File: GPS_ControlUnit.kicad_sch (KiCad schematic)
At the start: 0 parts

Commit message: MAX-M10S-00B
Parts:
- added ?: MAX-M10S-00B, symbol MAX-M10S-00B:MAX-M10S-00B
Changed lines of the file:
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@@
 (kicad_sch (version 20211123) (generator eeschema)
   (paper "A4")
+  (symbol (lib_id "MAX-M10S-00B:MAX-M10S-00B") (at 213.995 47.625 0) (unit 1)
+    (in_bom yes) (on_board yes) (fields_autoplaced)
+    (property "Reference" "?" (id 0) (at 235.585 34.29 0))
+    (property "Value" "MAX-M10S-00B" (id 1) (at 235.585 36.83 0))
+    (property "Footprint" "" (id 2) (at 213.995 47.625 0)
+      (effects (font (size 1.27 1.27)) hide)
+    )
+    (property "Datasheet" "" (id 3) (at 213.995 47.625 0)
+      (effects (font (size 1.27 1.27)) hide)
+    )
+    (property "Reference_1" "IC" (id 4) (at 235.585 39.37 0))
+    (property "Value_1" "MAX-M10S-00B" (id 5) (at 235.585 41.91 0))
+    (property "Footprint_1" "MAXM10S00B" (id 6) (at 253.365 142.545 0)
+      (effects (font (size 1.27 1.27)) (justify left top) hide)
+    )
+    (property "Datasheet_1" "https://content.u-blox.com/sites/default/files/MAX-M10S_IntegrationManual_UBX-20053088.pdf" (id 7) (at 253.365 242.545 0)
+      (effects (font (size 1.27 1.27)) (justify left top) hide)
+    )
+    (property "Height" "2.7" (id 8) (at 253.365 442.545 0)
+      (effects (font (size 1.27 1.27)) (justify left top) hide)
+    )
+    (property "Manufacturer_Name" "u-blox" (id 9) (at 253.365 542.545 0)
+      (effects (font (size 1.27 1.27)) (justify left top) hide)
+    )
+    (property "Manufacturer_Part_Number" "MAX-M10S-00B" (id 10) (at 253.365 642.545 0)
+      (effects (font (size 1.27 1.27)) (justify left top) hide)
+    )
+    (property "Mouser Part Number" "377-MAX-M10S-00B" (id 11) (at 253.365 742.545 0)
+      (effects (font (size 1.27 1.27)) (justify left top) hide)
+    )
+    (property "Mouser Price/Stock" "https://www.mouser.co.uk/ProductDetail/u-blox/MAX-M10S-00B?qs=A6eO%252BMLsxmT0PfQYPb7LLQ%3D%3D" (id 12) (at 253.365 842.545 0)
+      (effects (font (size 1.27 1.27)) (justify left top) hide)
+    )
+    (property "Arrow Part Number" "MAX-M10S-00B" (id 13) (at 253.365 942.545 0)
+      (effects (font (size 1.27 1.27)) (justify left top) hide)
+    )
+    (property "Arrow Price/Stock" "https://www.arrow.com/en/products/max-m10s-00b/u-blox?region=nac" (id 14) (at 253.365 1042.545 0)
+      (effects (font (size 1.27 1.27)) (justify left top) hide)
+    )
+    (pin "1")
+    (pin "10")
+    (pin "11")
+    (pin "12")
+    (pin "13")
+    (pin "14")
+    (pin "15")
+    (pin "16")
+    (pin "17")
+    (pin "18")
+    (pin "2")
+    (pin "3")
+    (pin "4")
+    (pin "5")
+    (pin "6")
+    (pin "7")
+    (pin "8")
+    (pin "9")
+  )
   (sheet (at 53.34 90.17) (size 59.055 36.195) (fields_autoplaced)
     (stroke (width 0.1524) (type solid) (color 0 0 0 0))

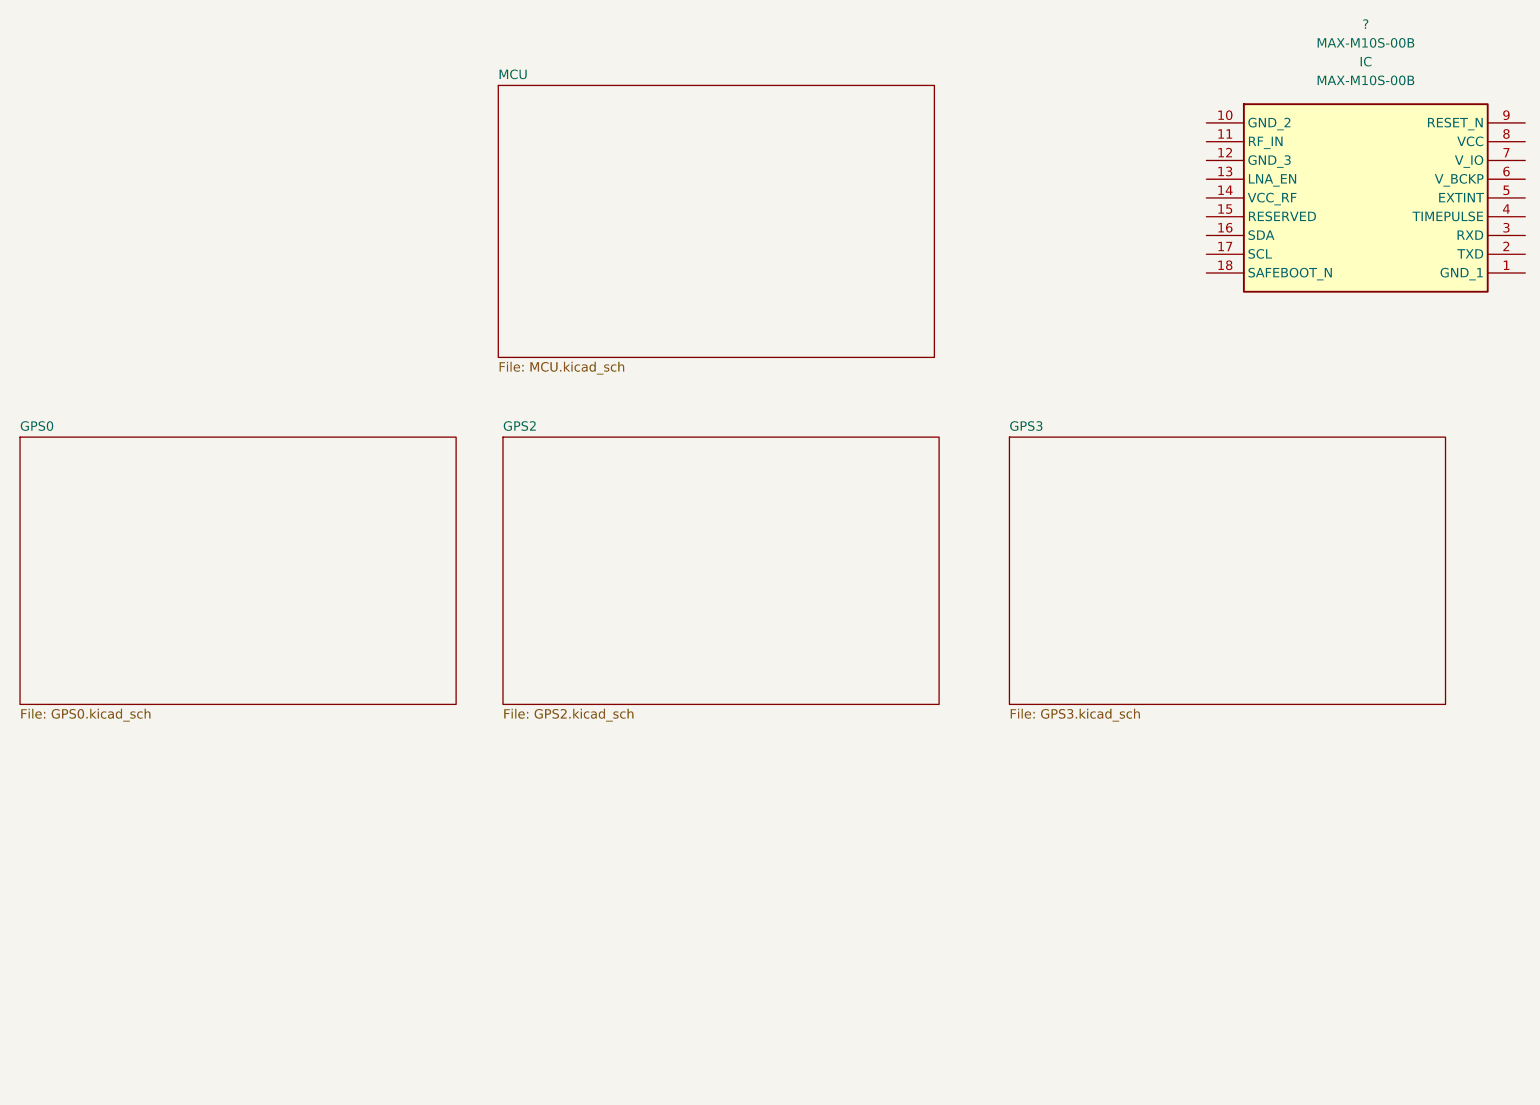
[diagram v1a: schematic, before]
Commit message: Adding M10
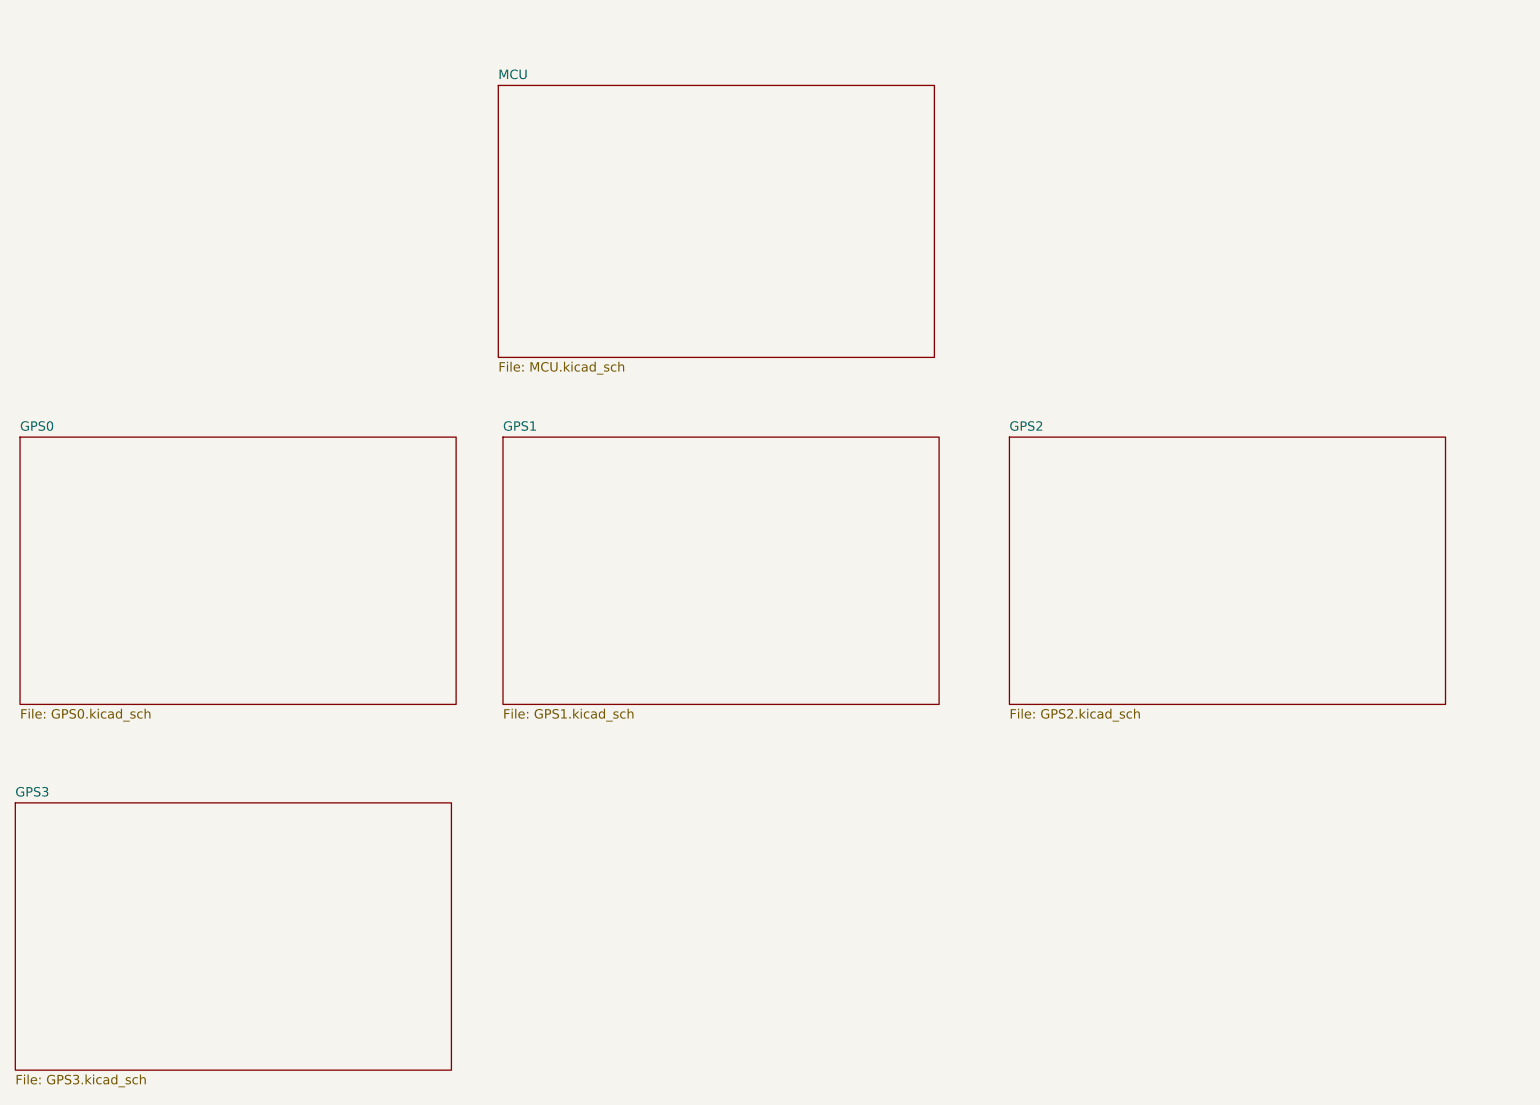
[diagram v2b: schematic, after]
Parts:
- removed ?: MAX-M10S-00B, symbol MAX-M10S-00B:MAX-M10S-00B
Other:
- added sheet GPS1 (GPS1.kicad_sch)
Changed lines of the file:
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@@
 (kicad_sch (version 20211123) (generator eeschema)
   (paper "A4")
-  (symbol (lib_id "MAX-M10S-00B:MAX-M10S-00B") (at 213.995 47.625 0) (unit 1)
-    (in_bom yes) (on_board yes) (fields_autoplaced)
-    (property "Reference" "?" (id 0) (at 235.585 34.29 0))
-    (property "Value" "MAX-M10S-00B" (id 1) (at 235.585 36.83 0))
-    (property "Footprint" "" (id 2) (at 213.995 47.625 0)
-      (effects (font (size 1.27 1.27)) hide)
-    )
-    (property "Datasheet" "" (id 3) (at 213.995 47.625 0)
-      (effects (font (size 1.27 1.27)) hide)
-    )
-    (property "Reference_1" "IC" (id 4) (at 235.585 39.37 0))
-    (property "Value_1" "MAX-M10S-00B" (id 5) (at 235.585 41.91 0))
-    (property "Footprint_1" "MAXM10S00B" (id 6) (at 253.365 142.545 0)
-      (effects (font (size 1.27 1.27)) (justify left top) hide)
-    )
-    (property "Datasheet_1" "https://content.u-blox.com/sites/default/files/MAX-M10S_IntegrationManual_UBX-20053088.pdf" (id 7) (at 253.365 242.545 0)
-      (effects (font (size 1.27 1.27)) (justify left top) hide)
-    )
-    (property "Height" "2.7" (id 8) (at 253.365 442.545 0)
-      (effects (font (size 1.27 1.27)) (justify left top) hide)
-    )
-    (property "Manufacturer_Name" "u-blox" (id 9) (at 253.365 542.545 0)
-      (effects (font (size 1.27 1.27)) (justify left top) hide)
-    )
-    (property "Manufacturer_Part_Number" "MAX-M10S-00B" (id 10) (at 253.365 642.545 0)
-      (effects (font (size 1.27 1.27)) (justify left top) hide)
-    )
-    (property "Mouser Part Number" "377-MAX-M10S-00B" (id 11) (at 253.365 742.545 0)
-      (effects (font (size 1.27 1.27)) (justify left top) hide)
-    )
-    (property "Mouser Price/Stock" "https://www.mouser.co.uk/ProductDetail/u-blox/MAX-M10S-00B?qs=A6eO%252BMLsxmT0PfQYPb7LLQ%3D%3D" (id 12) (at 253.365 842.545 0)
-      (effects (font (size 1.27 1.27)) (justify left top) hide)
-    )
-    (property "Arrow Part Number" "MAX-M10S-00B" (id 13) (at 253.365 942.545 0)
-      (effects (font (size 1.27 1.27)) (justify left top) hide)
-    )
-    (property "Arrow Price/Stock" "https://www.arrow.com/en/products/max-m10s-00b/u-blox?region=nac" (id 14) (at 253.365 1042.545 0)
-      (effects (font (size 1.27 1.27)) (justify left top) hide)
-    )
-    (pin "1")
-    (pin "10")
-    (pin "11")
-    (pin "12")
-    (pin "13")
-    (pin "14")
-    (pin "15")
-    (pin "16")
-    (pin "17")
-    (pin "18")
-    (pin "2")
-    (pin "3")
-    (pin "4")
-    (pin "5")
-    (pin "6")
-    (pin "7")
-    (pin "8")
-    (pin "9")
-  )
   (sheet (at 53.34 90.17) (size 59.055 36.195) (fields_autoplaced)
     (stroke (width 0.1524) (type solid) (color 0 0 0 0))
@@
     (stroke (width 0.1524) (type solid) (color 0 0 0 0))
     (fill (color 0 0 0 0.0000))
-    (property "Sheet name" "GPS3" (id 0) (at 187.325 89.4584 0)
+    (property "Sheet name" "GPS2" (id 0) (at 187.325 89.4584 0)
       (effects (font (size 1.27 1.27)) (justify left bottom))
     )
-    (property "Sheet file" "GPS3.kicad_sch" (id 1) (at 187.325 126.9496 0)
+    (property "Sheet file" "GPS2.kicad_sch" (id 1) (at 187.325 126.9496 0)
+      (effects (font (size 1.27 1.27)) (justify left top))
+    )
+  )
+  (sheet (at 52.705 139.7) (size 59.055 36.195) (fields_autoplaced)
+    (stroke (width 0.1524) (type solid) (color 0 0 0 0))
+    (fill (color 0 0 0 0.0000))
+    (property "Sheet name" "GPS3" (id 0) (at 52.705 138.9884 0)
+      (effects (font (size 1.27 1.27)) (justify left bottom))
+    )
+    (property "Sheet file" "GPS3.kicad_sch" (id 1) (at 52.705 176.4796 0)
       (effects (font (size 1.27 1.27)) (justify left top))
     )
@@
     (stroke (width 0.1524) (type solid) (color 0 0 0 0))
     (fill (color 0 0 0 0.0000))
-    (property "Sheet name" "GPS2" (id 0) (at 118.745 89.4584 0)
+    (property "Sheet name" "GPS1" (id 0) (at 118.745 89.4584 0)
       (effects (font (size 1.27 1.27)) (justify left bottom))
     )
-    (property "Sheet file" "GPS2.kicad_sch" (id 1) (at 118.745 126.9496 0)
+    (property "Sheet file" "GPS1.kicad_sch" (id 1) (at 118.745 126.9496 0)
       (effects (font (size 1.27 1.27)) (justify left top))
     )

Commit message: First commit
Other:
- added sheet GPS_Tracker (GPS_Tracker.kicad_sch)
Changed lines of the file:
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@@
+    )
+  )
+  (sheet (at 187.325 41.91) (size 59.69 37.465) (fields_autoplaced)
+    (stroke (width 0.1524) (type solid) (color 0 0 0 0))
+    (fill (color 0 0 0 0.0000))
+    (property "Sheet name" "GPS_Tracker" (id 0) (at 187.325 41.1984 0)
+      (effects (font (size 1.27 1.27)) (justify left bottom))
+    )
+    (property "Sheet file" "GPS_Tracker.kicad_sch" (id 1) (at 187.325 79.9596 0)
+      (effects (font (size 1.27 1.27)) (justify left top))
     )
   )
